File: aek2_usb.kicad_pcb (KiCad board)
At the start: 2 copper layers, 439 x 141.6 mm, 240 parts, among them J2 Conn_01x04, J3 Conn_01x04, U1 ATmega32A-PU

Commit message: change logo
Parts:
- added G***: LOGO, custom_parts:pear_x_elmo_copper, F.Cu at (189.2, 147.8)
- G***: moved to B.Cu
- moved G*** 223.9 mm to (407.0, 208.0), turned to 180 degrees

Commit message: cleanup
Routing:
- net Net-(D109-Pad2): track 13.3 -> 14.1 mm
- net Net-(D105-Pad2): track 13.5 -> 14.2 mm
- net Net-(D98-Pad2): track 13.4 -> 14.1 mm
- net Net-(D97-Pad2): track 13.4 -> 14.1 mm
- net Net-(D107-Pad2): track 13.4 -> 14.1 mm
- net Net-(D113-Pad2): track 13.5 -> 14.3 mm
- net Net-(D104-Pad2): track 15.0 -> 15.7 mm
- net Net-(D96-Pad2): track 13.6 -> 14.2 mm
- net Net-(D99-Pad2): track 13.5 -> 14.1 mm
- net Net-(D111-Pad2): track 13.4 -> 14.0 mm
- net Net-(D110-Pad2): track 13.3 -> 13.9 mm
- net Net-(D103-Pad2): track 15.0 -> 15.6 mm
- net Net-(D100-Pad2): track 13.5 -> 14.1 mm

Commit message: Update aek2_usb.kicad_pcb
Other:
- board text added: "github.com/kb-elmo/aek2_usb elmo.space"

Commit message: added firmware
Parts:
- renumbered Boot to Boot1, D11 to D10, D107 to D100, D96 to D101, D101 to D102, D109 to D105, D108 to D106, D87 to D107, D12 to D11, D14 to D12, D15 to D13, D16 to D14, D17 to D15, D18 to D16, D19 to D17, D20 to D18, D21 to D19, D22 to D20, D23 to D21, D24 to D22, D25 to D23, D26 to D24, D27 to D25, D28 to D26, D29 to D27, D30 to D28, D31 to D29, D32 to D30, D33 to D31, D34 to D32, D35 to D33, D36 to D34, D37 to D35, D38 to D36, D39 to D37, D40 to D38, D41 to D39, D5 to D4, D42 to D40, D43 to D41, D44 to D42, D45 to D43, D46 to D44, D47 to D45, D48 to D46, D49 to D47, D50 to D48, D51 to D49, D6 to D5, D52 to D50, D53 to D51, D54 to D52, D55 to D53, D56 to D54, D57 to D55, D58 to D56, D59 to D57, D60 to D58, D61 to D59, D7 to D6, D62 to D60, D63 to D61, D64 to D62, D65 to D63, D66 to D64, D67 to D65, D68 to D66, D69 to D67, D72 to D68, D73 to D69, D8 to D7, D74 to D70, D75 to D71, D78 to D72, D76 to D73, D80 to D74, D79 to D75, D77 to D76, D83 to D77, D84 to D78, D86 to D79, D9 to D8, D92 to D80, D95 to D81, D97 to D82, D98 to D83, D100 to D84, D114 to D85, D90 to D86, D102 to D87, D91 to D88, D111 to D89, D10 to D9, D110 to D90, D105 to D91, D89 to D92, D88 to D93, D93 to D95, D112 to D96, D99 to D97, D106 to D98, D113 to D99, H2 to H1, H1 to H2, J3 to J1, MX12 to MX10, MX99 to MX100, MX107 to MX103, MX106 to MX104, MX85 to MX105, MX13 to MX11, MX14 to MX12, MX15 to MX13, MX16 to MX14, MX17 to MX15, MX18 to MX16, MX19 to MX17, MX20 to MX18, MX21 to MX19, MX3 to MX2, MX22 to MX20, MX23 to MX21, MX24 to MX22, MX25 to MX23, MX26 to MX24, MX27 to MX25, MX28 to MX26, MX29 to MX27, MX30 to MX28, MX31 to MX29, MX4 to MX3, MX32 to MX30, MX33 to MX31, MX34 to MX32, MX35 to MX33, MX36 to MX34, MX37 to MX35, MX38 to MX36, MX39 to MX37, MX40 to MX38, MX41 to MX39, MX5 to MX4, MX42 to MX40, MX43 to MX41, MX44 to MX42, MX45 to MX43, MX46 to MX44, MX47 to MX45, MX48 to MX46, MX49 to MX47, MX50 to MX48, MX51 to MX49, MX6 to MX5, MX52 to MX50, MX53 to MX51, MX54 to MX52, MX55 to MX53, MX56 to MX54, MX57 to MX55, MX58 to MX56, MX59 to MX57, MX60 to MX58, MX61 to MX59, MX7 to MX6, MX62 to MX60, MX63 to MX61, MX64 to MX62, MX65 to MX63, MX66 to MX64, MX67 to MX65, MX70 to MX66, MX71 to MX67, MX72 to MX68, MX73 to MX69, MX8 to MX7, MX76 to MX70, MX74 to MX71, MX78 to MX72, MX77 to MX73, MX75 to MX74, MX81 to MX75, MX82 to MX76, MX84 to MX77, MX90 to MX78, MX93 to MX79, MX9 to MX8, MX95 to MX80, MX96 to MX81, MX98 to MX82, MX112 to MX83, MX88 to MX84, MX100 to MX85, MX89 to MX86, MX109 to MX87, MX108 to MX88, MX103 to MX89, MX10 to MX9, MX87 to MX90, MX86 to MX91, MX91 to MX93, MX110 to MX94, MX97 to MX95, MX104 to MX96, MX111 to MX97, MX105 to MX98, MX94 to MX99, Reset to Reset1

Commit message: update readme
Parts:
- moved C3 0.51 mm to (316.5, 152.5)
- moved C2 0.38 mm to (316.5, 143.4)
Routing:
- net +5V: track 449.0 -> 449.6 mm

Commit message: added ISO support (UNTESTED!)
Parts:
- added D108: D_Small, custom_parts:D_DO-35_SOD27_P7.62mm_Horizontal, F.Cu at (128.0, 227.8)
- added MX106: MX-NoLED, Alps_Only:ALPS-1.25U, F.Cu at (97.0, 224.8)
- added MX107: MX-NoLED, Alps_Only:ALPS-1U, F.Cu at (337.3, 205.8)
- added MX108: MX-NoLED, Alps_Only:ALPS-2U, F.Cu at (358.8, 196.3)
- added MX109: MX-NoLED, Alps_Only:ALPS-1U, F.Cu at (118.4, 224.7)
- MX100, MX102, MX26: footprint Alps_Only:ALPS-1U -> Alps_Only:ALPS-2U
- MX27, MX40, MX67, MX69, MX75, MX77: footprint Alps_Only:ALPS-1U -> Alps_Only:ALPS-1.5U
- MX41: footprint Alps_Only:ALPS-1U -> Alps_Only:ALPS-1.75U
- MX54, MX55: footprint Alps_Only:ALPS-1U -> Alps_Only:ALPS-2.25U
- MX66: footprint Alps_Only:ALPS-1U -> Alps_Only:ALPS-2.75U
- MX68, MX76: footprint Alps_Only:ALPS-1U -> Alps_Only:ALPS-1.25U
- moved D57 26.4 mm to (89.8, 227.7)
- moved D56 10.2 mm to (369.2, 208.9)
- moved D42 1.21 mm to (367.2, 189.9)
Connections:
- net Net-(D42-Pad2) renamed iso_sls
- net Net-(D56-Pad2) renamed iso_ent
- net Net-(D57-Pad2) renamed split_shift
- MX56 pad 1: col1 -> col2
- MX57 pad 1: col2 -> col3
- MX58 pad 1: col3 -> col4
- MX59 pad 1: col4 -> col5
- MX60 pad 1: col5 -> col6
- MX61 pad 1: col6 -> col7
- MX62 pad 1: col7 -> col8
- MX63 pad 1: col8 -> col9
- MX64 pad 1: col9 -> col10
- MX65 pad 1: col10 -> col11
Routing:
- net iso_sls: track 7.28 -> 50.5 mm
- net col5: track 621.0 -> 656.4 mm
- net row4: track 332.8 -> 362.6 mm
- net col2: track 548.1 -> 571.2 mm
- net col10: track 517.8 -> 540.8 mm
- net col3: track 576.2 -> 596.5 mm
- net col6: track 800.0 -> 819.1 mm
- net col7: track 823.5 -> 842.7 mm
- net col4: track 560.6 -> 579.6 mm
- net col8: track 733.7 -> 752.7 mm
- net col9: track 641.0 -> 659.9 mm
- net split_shift: track 7.16 -> 24.6 mm
- net col1: track 485.7 -> 502.6 mm
- net iso_ent: track 7.28 -> 22.2 mm
- net col0: track 504.3 -> 516.3 mm
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
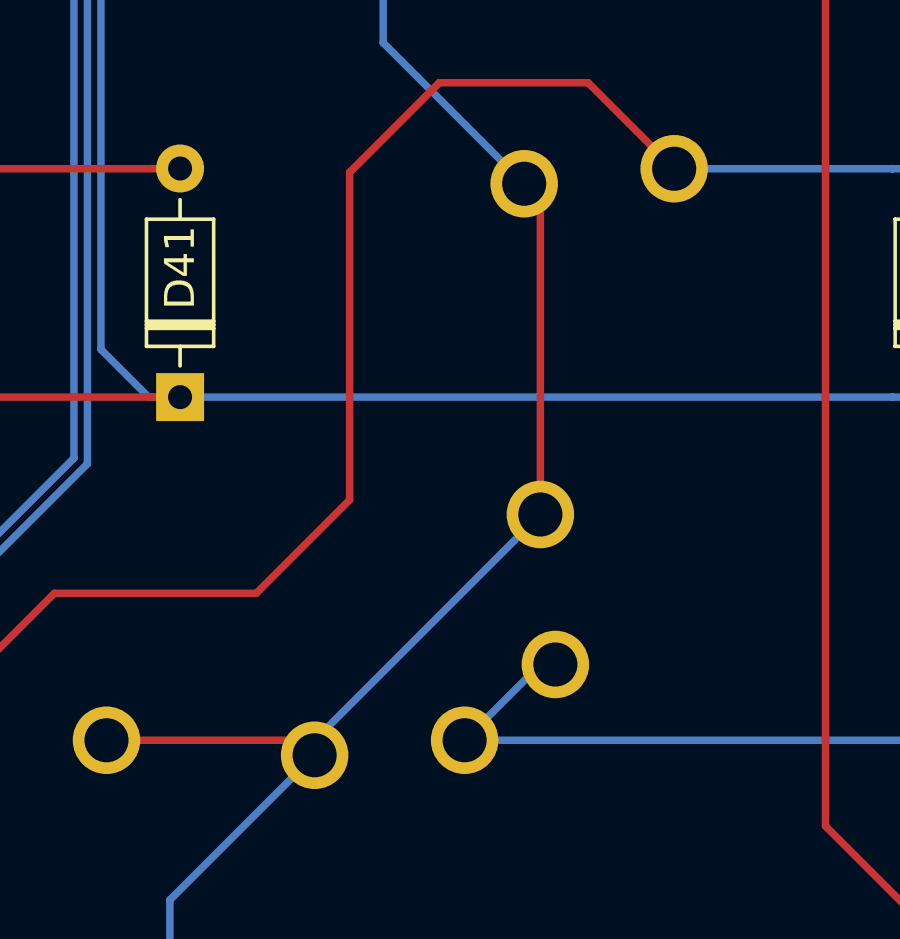
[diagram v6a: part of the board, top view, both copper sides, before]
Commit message: fix ISO enter position (still untested!)
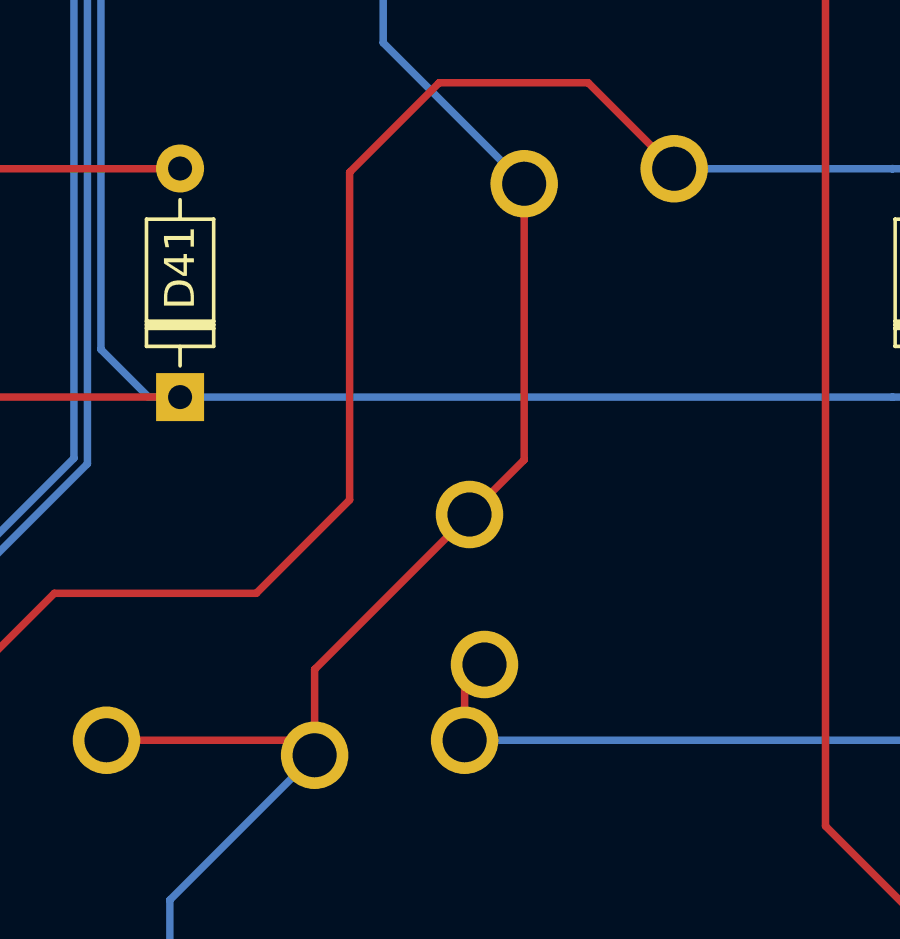
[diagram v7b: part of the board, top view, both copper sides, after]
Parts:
- moved MX108 2.36 mm to (356.4, 196.3)
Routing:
- net iso_ent: track 22.2 -> 20.9 mm
